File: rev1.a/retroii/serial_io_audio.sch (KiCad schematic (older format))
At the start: 62 parts, among them J13 74LS74, J14 Game_IO_Socket, J2 Joystick 1, J24 Headphone, J3 Joystick 2, J4 PC Port 1, J5 PC Port 2, J6 Edge mounted connector, J7 Cassette In, J8 Cassette Out, J9 Speaker Jack, K13 LM741, Q4 MPSA13, U2 NE556, U7 NE556

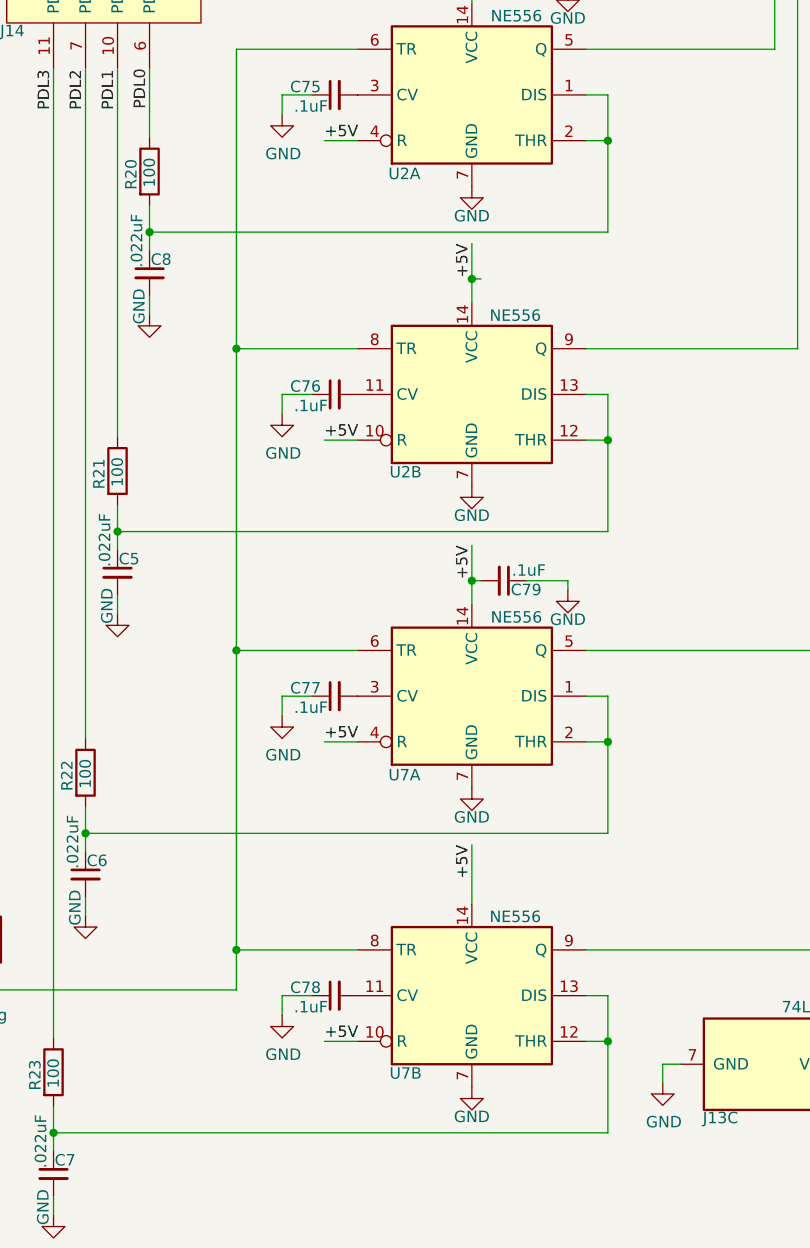
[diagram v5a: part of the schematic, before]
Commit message: added series resistors for prop 5v interface pins.
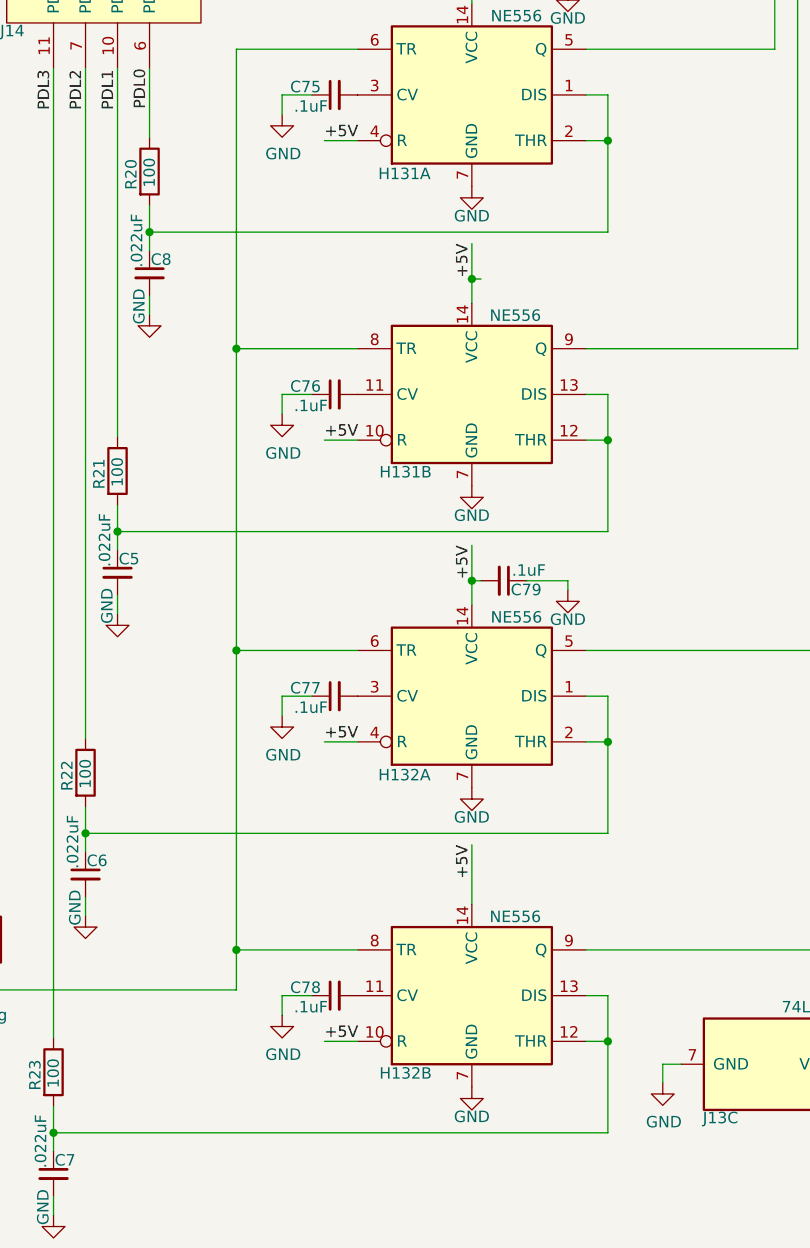
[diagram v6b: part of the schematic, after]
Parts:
- renumbered U2 to H131, U7 to H132
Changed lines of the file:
@@
 Connection ~ 10140 4770
 $Comp
-L Timer:NE556 U2
+L Timer:NE556 H131
 U 1 1 5CCBC03B
 P 4780 2960
-F 0 "U2" H 4485 2615 50  0000 C CNN
+F 0 "H131" H 4485 2615 50  0000 C CNN
 F 1 "NE556" H 4975 3305 50  0000 C CNN
 F 2 "retroii_footprints:DIP-14_W7.62mm_Socket_LongPads" H 4780 2960 50  0001 C CNN
@@
 	3795 2145 4060 2145
 $Comp
-L Timer:NE556 U2
+L Timer:NE556 H131
 U 2 1 5CCD9CE9
 P 4780 4270
-F 0 "U2" H 4490 3930 50  0000 C CNN
+F 0 "H131" H 4490 3930 50  0000 C CNN
 F 1 "NE556" H 4970 4615 50  0000 C CNN
 F 2 "retroii_footprints:DIP-14_W7.62mm_Socket_LongPads" H 4780 4270 50  0001 C CNN
@@
 $EndComp
 $Comp
-L Timer:NE556 U7
+L Timer:NE556 H132
 U 1 1 5CDCD2A0
 P 4780 5590
-F 0 "U7" H 4485 5245 50  0000 C CNN
+F 0 "H132" H 4485 5245 50  0000 C CNN
 F 1 "NE556" H 4975 5935 50  0000 C CNN
 F 2 "retroii_footprints:DIP-14_W7.62mm_Socket_LongPads" H 4780 5590 50  0001 C CNN
@@
 $EndComp
 $Comp
-L Timer:NE556 U7
+L Timer:NE556 H132
 U 2 1 5CDCD2A6
 P 4780 6900
-F 0 "U7" H 4490 6560 50  0000 C CNN
+F 0 "H132" H 4490 6560 50  0000 C CNN
 F 1 "NE556" H 4970 7245 50  0000 C CNN
 F 2 "retroii_footprints:DIP-14_W7.62mm_Socket_LongPads" H 4780 6900 50  0001 C CNN

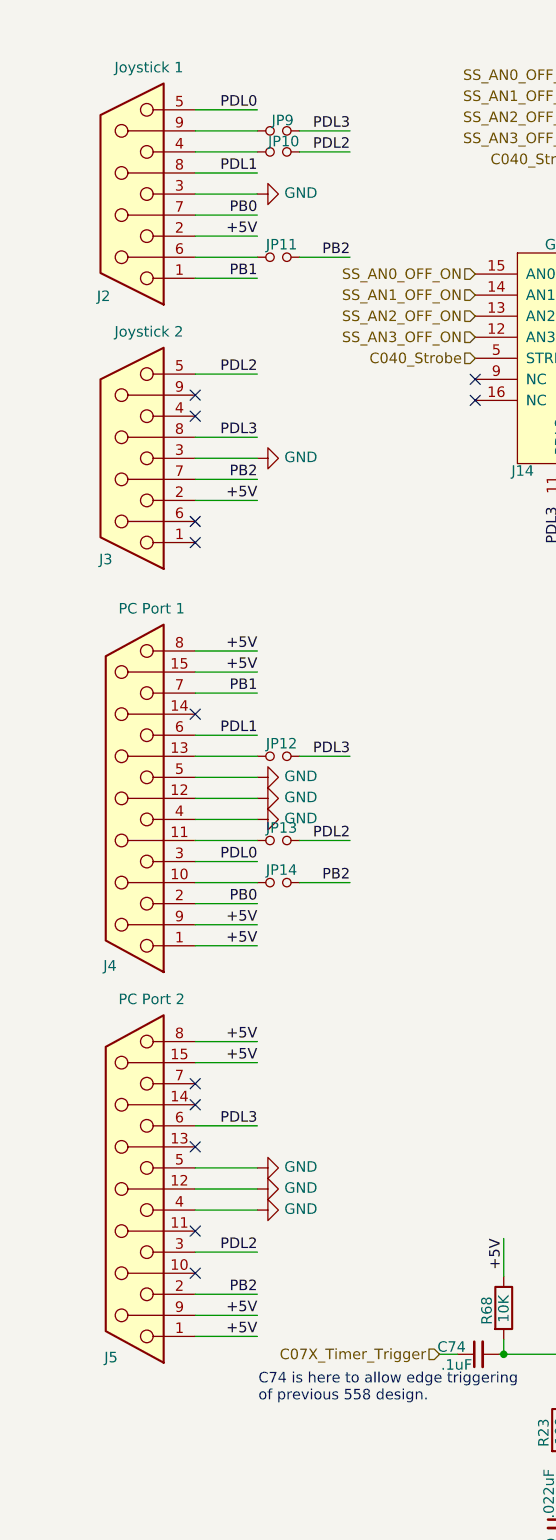
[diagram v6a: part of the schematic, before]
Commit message: replaced db9/db15 connectors with stacked versions
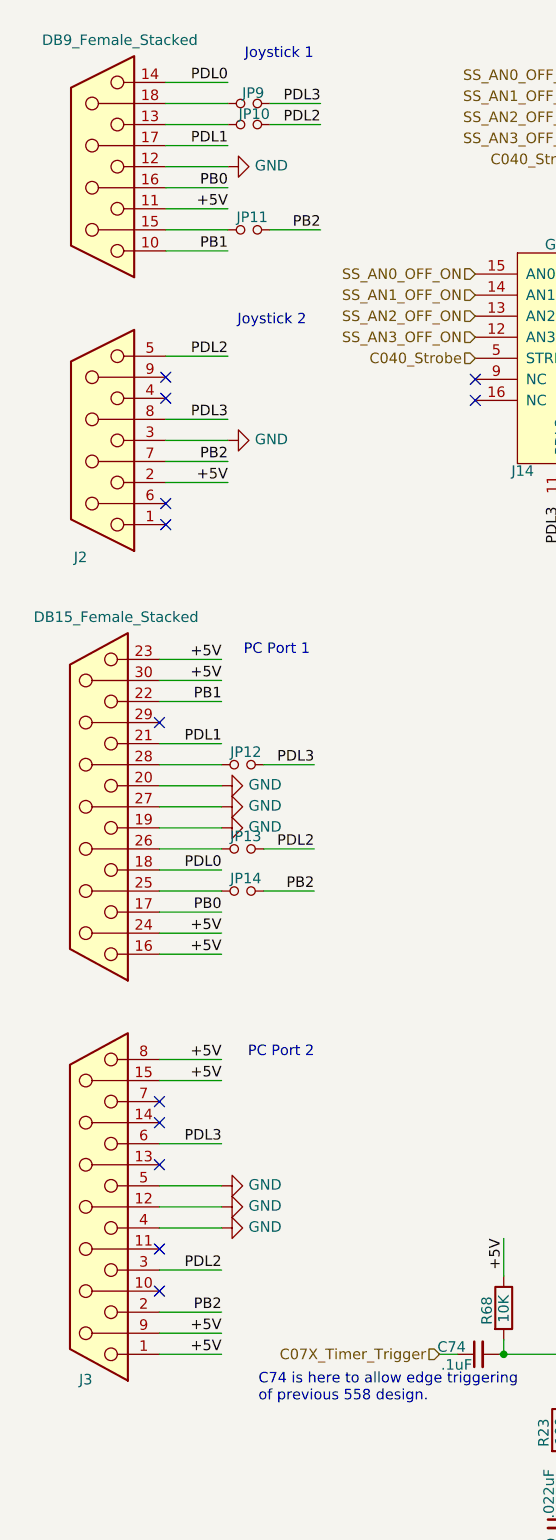
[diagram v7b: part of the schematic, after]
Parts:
- removed J2: Joystick 1, retroii_footprints:Amphenol_DSUB9_D09S33E6GV00LF, symbol Connector:DB9_Female
- removed J3: Joystick 2, retroii_footprints:Amphenol_DSUB9_D09S33E6GV00LF, symbol Connector:DB9_Female
- removed J4: PC Port 1, retroii_footprints:Amphenol_DSUB9_D15S33E4GV00LF, symbol Connector:DB15_Female
- removed J5: PC Port 2, retroii_footprints:Amphenol_DSUB9_D15S33E4GV00LF, symbol Connector:DB15_Female
- added J2: DB9_Female_Stacked, retroii_footprints:Amphenol_L17H2220131, symbol retroii:DB9_Female_Stacked
- added J3: DB15_Female_Stacked, retroii_footprints:Amphenol_L17H2440131, symbol retroii:DB15_Female_Stacked
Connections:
- net +5V: now also J2.11, J2.2, J3.1, J3.15 (P15), J3.16, J3.23, J3.24, J3.30, J3.8, J3.9 (P9)
- net GND: now also J2.12, J2.3, J3.12 (P12), J3.19, J3.20, J3.27, J3.4, J3.5
- net PB0: now also J2.16, J3.17
- net PB1: now also J2.10, J3.22
- net PB2: now also J2.7, J3.2
- net PDL0: now also J2.14, J3.18
- net PDL1: now also J2.17, J3.21
- net PDL2: now also J2.5, J3.3
- net PDL3: now also J2.8, J3.6
- net at JP10.1: now also J2.13
- net at JP11.1: now also J2.15
- net at JP9.1: now also J2.18
- net at JP14.1: now also J3.25
- net at JP13.1: now also J3.26
- net at JP12.1: now also J3.28
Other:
- note added: "Joystick 1"
- note added: "Joystick 2"
- note added: "PC Port 1"
- note added: "PC Port 2"
- moved on the sheet: JP10, JP11, JP12, JP13, JP14, JP9

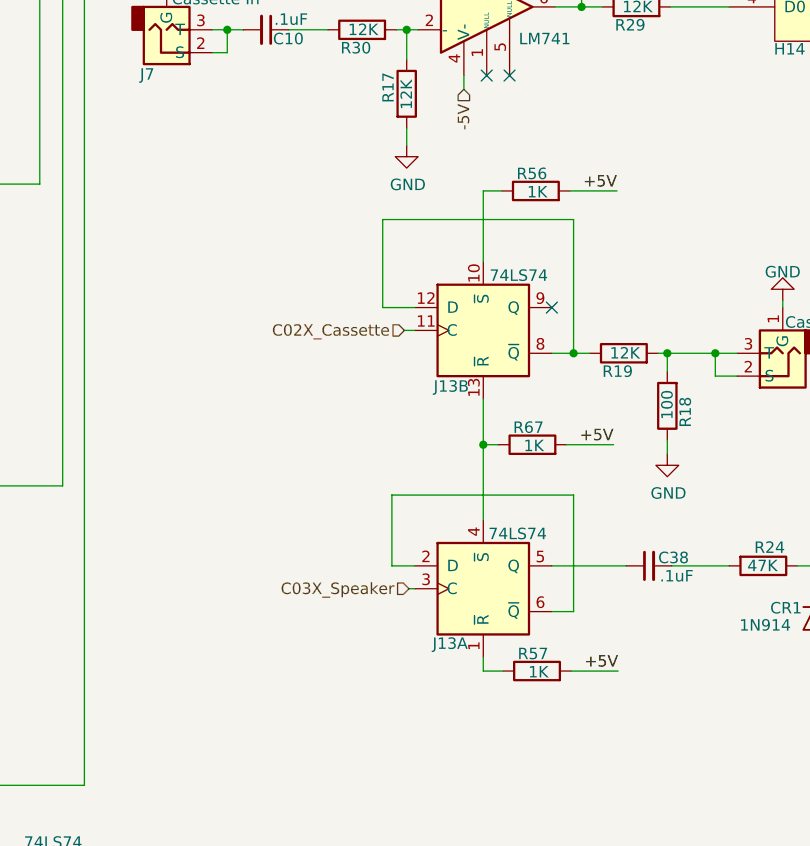
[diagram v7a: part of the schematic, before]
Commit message: laying out audio
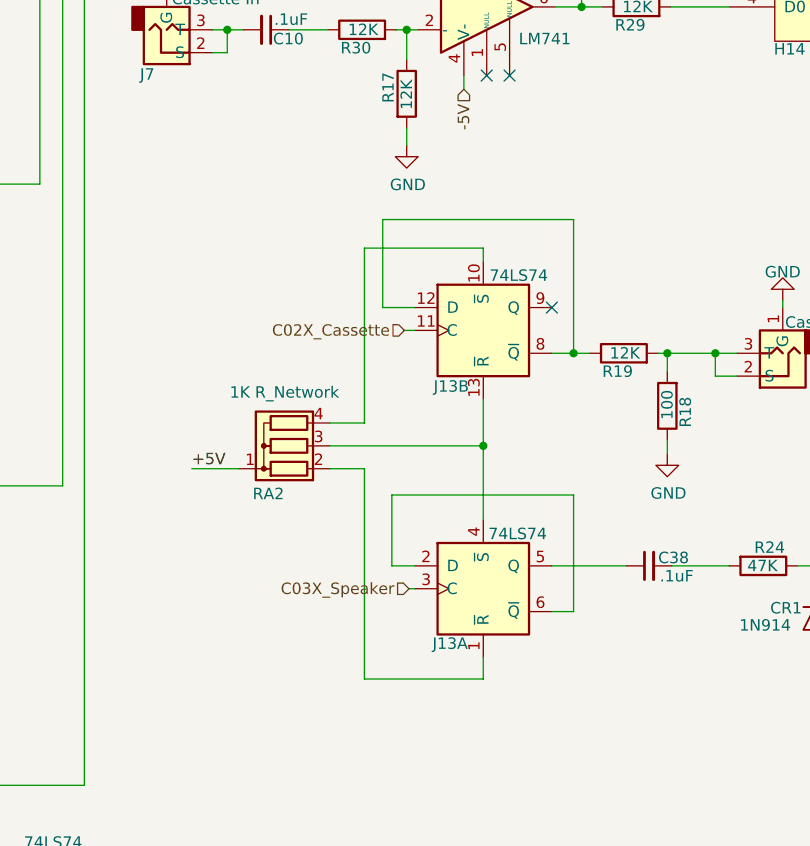
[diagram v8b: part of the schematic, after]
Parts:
- removed R56, R57, R67: 1K, retroii_footprints:R_Axial_DIN0207_L6.3mm_D2.5mm_P10.16mm_Horizontal, symbol 6502:R
- added RA2: 1K R_Network, Resistor_THT:R_Array_SIP4, symbol Device:R_Network03
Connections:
- net +5V: now also RA2.1 (common)
- net at J13.1 (~R): now also RA2.2 (R1)
- net at J13.13 (~R), J13.4 (~S): now also RA2.3 (R2)
- net at J13.10 (~S): now also RA2.4 (R3)
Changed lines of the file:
@@
 Wire Wire Line
 	8610 4810 8540 4810
-Wire Wire Line
-	8145 5010 8145 5210
 $Comp
 L Device:C_Small C38
@@
 NoConn ~ 10200 3730
 $Comp
-L 6502:R R56
-U 1 1 5CCAFCB4
-P 8375 4100
-F 0 "R56" V 8450 4050 50  0000 L CNN
-F 1 "1K" V 8370 4050 50  0000 L CNN
-F 2 "retroii_footprints:R_Axial_DIN0207_L6.3mm_D2.5mm_P10.16mm_Horizontal" V 8305 4100 30  0001 C CNN
-F 3 "" H 8375 4100 30  0000 C CNN
-	1    8375 4100
-	0    -1   -1   0
-$EndComp
-Wire Wire Line
-	8525 4100 8730 4100
-Text Label 8730 4100 2    50   ~ 0
-+5V
-Wire Wire Line
-	8145 4410 8145 4100
-Wire Wire Line
-	8145 4100 8225 4100
-$Comp
-L 6502:R R57
-U 1 1 5CCC6EE7
-P 8380 6200
-F 0 "R57" V 8455 6150 50  0000 L CNN
-F 1 "1K" V 8375 6150 50  0000 L CNN
-F 2 "retroii_footprints:R_Axial_DIN0207_L6.3mm_D2.5mm_P10.16mm_Horizontal" V 8310 6200 30  0001 C CNN
-F 3 "" H 8380 6200 30  0000 C CNN
-	1    8380 6200
-	0    -1   -1   0
-$EndComp
-Wire Wire Line
-	8530 6200 8735 6200
-Text Label 8735 6200 2    50   ~ 0
-+5V
-Wire Wire Line
-	8230 6200 8145 6200
-Wire Wire Line
-	8145 6200 8145 6140
-$Comp
 L 74xx:74LS74 J13
 U 3 1 5CD2FA67
@@
 Wire Wire Line
 	6585 7200 6775 7200
-$Comp
-L 6502:R R67
-U 1 1 5CE48ADE
-P 8360 5210
-F 0 "R67" V 8435 5160 50  0000 L CNN
-F 1 "1K" V 8355 5160 50  0000 L CNN
-F 2 "retroii_footprints:R_Axial_DIN0207_L6.3mm_D2.5mm_P10.16mm_Horizontal" V 8290 5210 30  0001 C CNN
-F 3 "" H 8360 5210 30  0000 C CNN
-	1    8360 5210
-	0    -1   -1   0
-$EndComp
-Wire Wire Line
-	8510 5210 8715 5210
-Text Label 8715 5210 2    50   ~ 0
-+5V
-Wire Wire Line
-	8210 5210 8145 5210
-Connection ~ 8145 5210
-Wire Wire Line
-	8145 5210 8145 5540
 $Comp
 L Device:Jumper_NC_Small JP19
@@
 Text Notes 1465 5470 0    50   ~ 0
 PC Port 2
+$Comp
+L Device:R_Network03 RA2
+U 1 1 5D4AD33A
+P 7275 5215
+F 0 "RA2" V 7065 5285 50  0000 C CNN
+F 1 "1K R_Network" V 7509 5215 50  0000 C CNN
+F 2 "Resistor_THT:R_Array_SIP4" V 7550 5215 50  0001 C CNN
+F 3 "http://www.vishay.com/docs/31509/csc.pdf" H 7275 5215 50  0001 C CNN
+	1    7275 5215
+	0    -1   -1   0
+$EndComp
+Wire Wire Line
+	6870 5315 7075 5315
+Text Label 6870 5315 0    50   ~ 0
++5V
+Wire Wire Line
+	8145 5010 8145 5215
+Wire Wire Line
+	7475 5215 8145 5215
+Connection ~ 8145 5215
+Wire Wire Line
+	8145 5215 8145 5540
+Wire Wire Line
+	7475 5315 7625 5315
+Wire Wire Line
+	7625 5315 7625 6235
+Wire Wire Line
+	7625 6235 8145 6235
+Wire Wire Line
+	8145 6140 8145 6235
+Wire Wire Line
+	7625 5115 7625 4350
+Wire Wire Line
+	7625 4350 8145 4350
+Wire Wire Line
+	8145 4350 8145 4410
+Wire Wire Line
+	7475 5115 7625 5115
 Wire Bus Line
 	10690 2755 10690 3195
